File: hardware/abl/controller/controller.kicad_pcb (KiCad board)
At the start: 4 copper layers, 56.2 x 74 mm, 40 parts, among them IC2 FXL6408UMX, IC3 VEML6040A3OG, IC4 FXL6408UMX, J1 SFW20S-2STE1LF, J2 Conn_02x05_Odd_Even, J3 Conn_02x05_Odd_Even, J4 PRT-14417, J5 Conn_02x05_Odd_Even, Q2 AO3401A, Q4 AO3401A, U1 INA219AxD, U2 TXB0104RUT

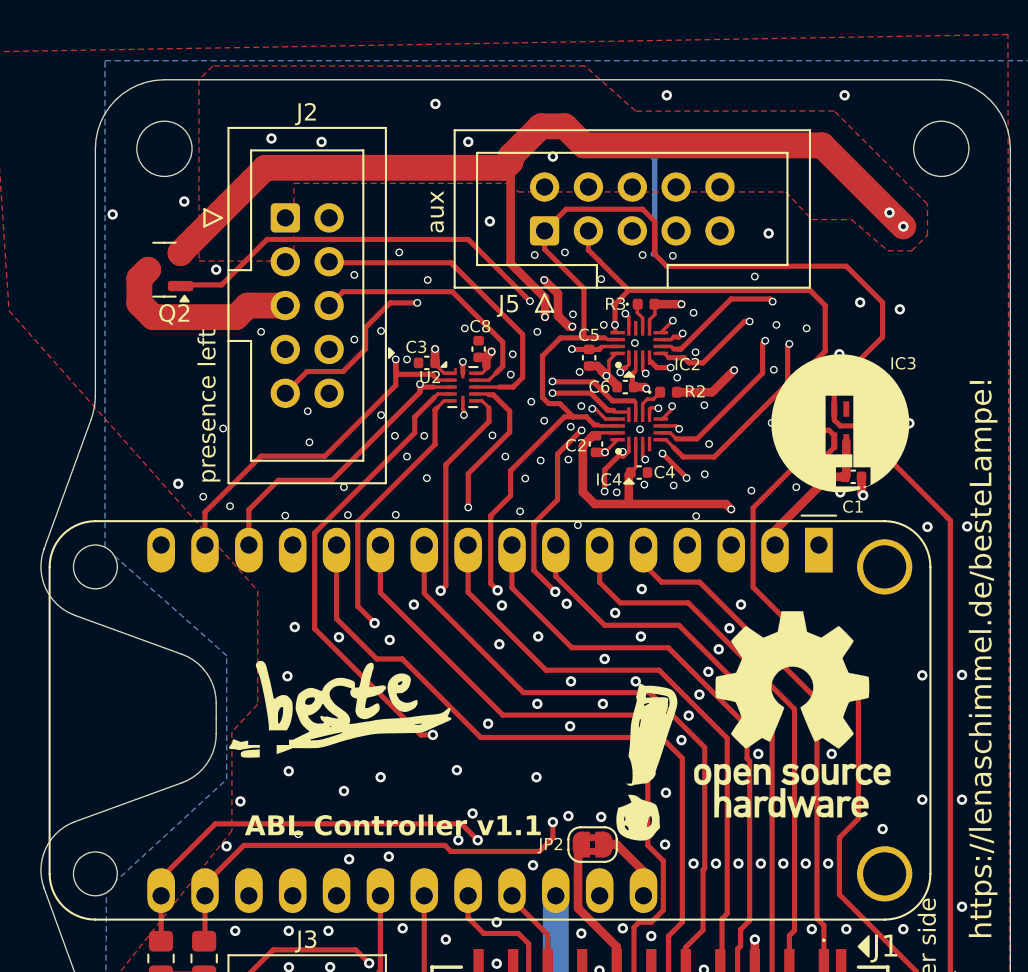
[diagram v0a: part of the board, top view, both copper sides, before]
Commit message: Exchanged GPIO Expander for one that supports 5V.
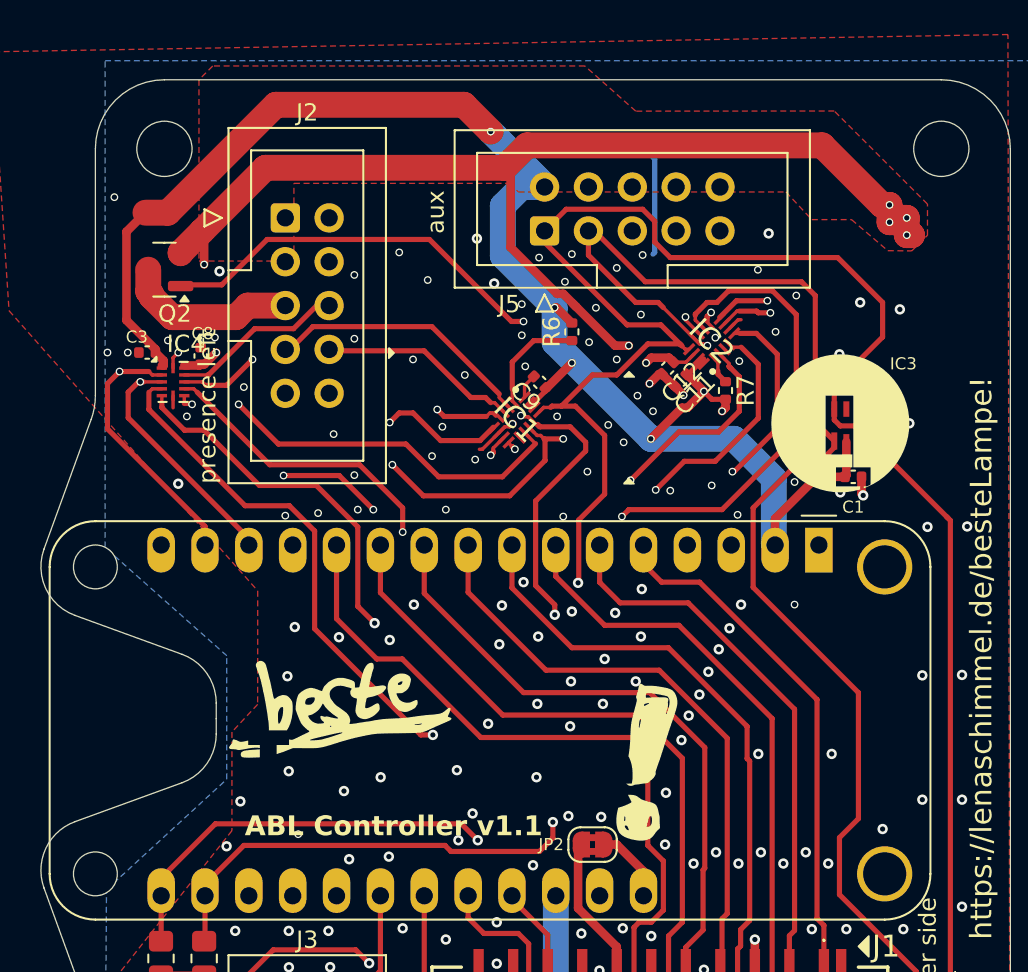
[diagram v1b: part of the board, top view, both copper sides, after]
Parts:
- removed C2, C4, C5, C6: 100nF, Capacitor_SMD:C_0402_1005Metric
- removed R2, R3: 4700R, LED_SMD:LED_0402_1005Metric
- removed REF**: OSHW-Logo_11.4x12mm_SilkScreen, Symbol:OSHW-Logo_11.4x12mm_SilkScreen
- removed U2: TXB0104RUT, Package_DFN_QFN:Texas_R-PUQFN-N12
- added C11: 100nF, Capacitor_SMD:C_0402_1005Metric, F.Cu at (96.9, 68.4)
- added C12: 100nF, Capacitor_SMD:C_0402_1005Metric, F.Cu at (96.2, 67.7)
- added C9: 100nF, Capacitor_SMD:C_0402_1005Metric, F.Cu at (88.7, 68.5)
- added IC1: TCA6408ARSVR, FXL6408UMX:QFN40P180X260X55-16N, F.Cu at (87.4, 70.7)
- added R6: 4700R, Resistor_SMD:R_0402_1005Metric, F.Cu at (90.6, 65.6)
- added R7: 4700R, Resistor_SMD:R_0402_1005Metric, F.Cu at (99.5, 69.0)
- IC2: value FXL6408UMX -> TCA6408ARSVR
- IC4: value FXL6408UMX -> TXB0104RUT; footprint FXL6408UMX:QFN40P180X260X55-16N -> Package_DFN_QFN:Texas_R-PUQFN-N12
- moved IC4 27.1 mm to (67.5, 68.5), turned to 0 degrees
- moved C3 16.2 mm to (66.0, 66.8)
- moved C8 16.1 mm to (69.1, 67.0)
- moved IC2 4.20 mm to (98.7, 66.2), turned to 135 degrees
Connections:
- IC2 pad 1: /GP_INT -> Net-(IC2-~{RESET})
- IC2 pad 10: Net-(IC2-/RST) -> /FX_5_7
- IC2 pad 11: /FX_5_1 -> /GP_INT
- IC2 pad 12: /FX_5_0 -> /SCL
- IC2 pad 13: /SCL -> /SDA
- IC2 pad 14: /SDA -> +5V
- IC2 pad 16: GND -> +3.3V
- IC2 pad 2: +5V -> /FX_5_0
- IC2 pad 3: /FX_5_7 -> /FX_5_1
- IC2 pad 4: /FX_5_6 -> /FX_5_2
- IC2 pad 5: /FX_5_5 -> /FX_5_3
- IC2 pad 6: /FX_5_4 -> GND
- IC2 pad 7: /FX_5_3 -> /FX_5_4
- IC2 pad 8: /FX_5_2 -> /FX_5_5
- IC2 pad 9: +3.3V -> /FX_5_6
- IC4 pad 1: /GP_INT -> +3.3V
- IC4 pad 10: Net-(IC4-/RST) -> /TX_L_5
- IC4 pad 11: /FX_3_1 -> +5V
- IC4 pad 12: /FX_3_0 -> /EN_UART
- IC4 pad 2: +3.3V -> /TX_L
- IC4 pad 3: /EN_UART -> /RX_L
- IC4 pad 4: /FX_3_6 -> /TX_R
- IC4 pad 5: /FX_3_5 -> /RX_R
- IC4 pad 6: /FX_3_4 -> GND
- IC4 pad 7: /FX_3_3 -> /RX_R_5
- IC4 pad 8: /FX_3_2 -> /TX_R_5
- IC4 pad 9: GND -> /RX_L_5
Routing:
- net +3.3V: track 110.2 -> 162.7 mm, vias 12 -> 11
- net /SCL: track 178.6 -> 193.9 mm, vias 5 -> 4
- net /FX_3_2: track 72.7 -> 58.1 mm
- net /FX_5_7: track 67.2 -> 81.3 mm, vias 4 -> 2
- net /FX_3_5: track 32.9 -> 19.0 mm
- net /FX_3_0: track 28.2 -> 15.5 mm, vias 1 -> 0
- net /FX_3_3: track 75.4 -> 62.9 mm
- net /RX_R_5: track 48.5 -> 57.9 mm, vias 1 -> 3
- net /FX_5_0: track 28.6 -> 38.0 mm, vias 2 -> 1
- net /FX_3_1: track 21.6 -> 12.4 mm, vias 1 -> 0
- net /EN_UART: track 18.6 -> 26.4 mm
- net GND: track 23.7 -> 31.1 mm, vias 224 -> 206
- net /GP_INT: track 31.1 -> 38.5 mm
- net Net-(IC1-~{RESET}): track 0.00 -> 6.27 mm
- net /FX_3_4: track 20.6 -> 26.2 mm
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
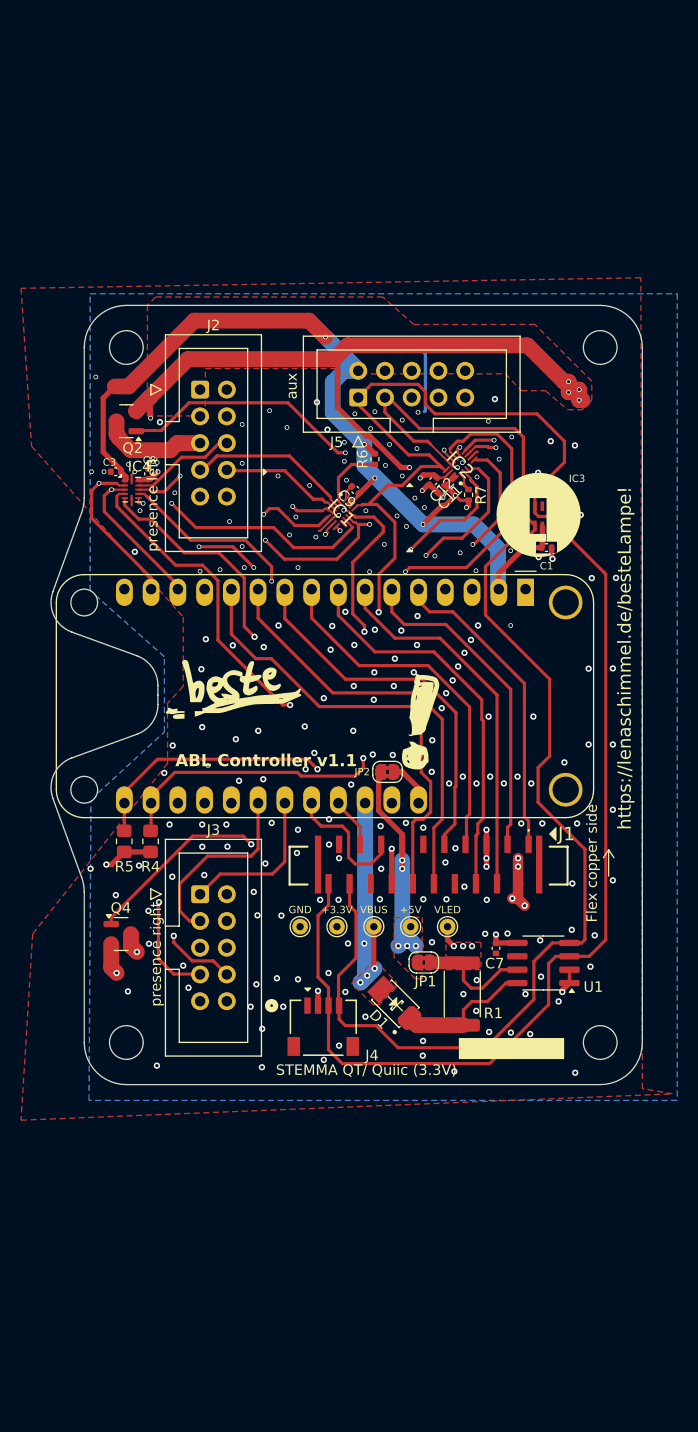
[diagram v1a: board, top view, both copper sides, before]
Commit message: Re-routed power, much cleanup.
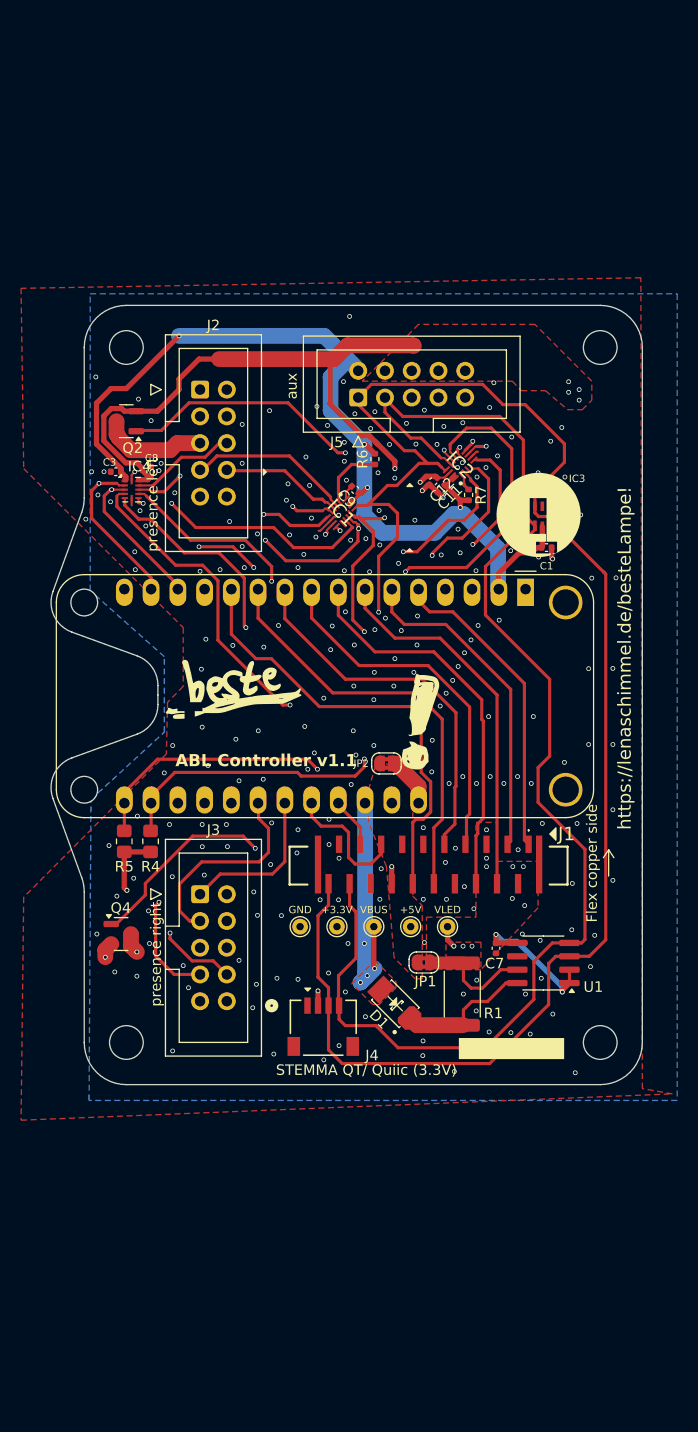
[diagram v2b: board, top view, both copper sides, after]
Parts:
- moved JP2 0.81 mm to (91.7, 94.5)
- moved C8 0.28 mm to (69.3, 66.8)
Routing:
- net GND: track 31.1 -> 9.55 mm, vias 206 -> 224
- net +5V: track 104.1 -> 113.5 mm, vias 14 -> 7
- net +4V: track 21.6 -> 12.8 mm
- net /SCL: track 193.9 -> 188.3 mm
- net +3.3V: track 162.7 -> 158.9 mm, vias 11 -> 9
- net /FX_5_5: track 10.6 -> 7.19 mm
- net /FX_5_4: track 12.8 -> 10.2 mm
- net +BATT: track 4.36 -> 6.08 mm
- net /SDA: track 201.6 -> 200.3 mm
- net /FX_3_3: track 62.9 -> 61.9 mm
- net /FX_5_7: track 81.3 -> 82.2 mm
- net /RX_R: track 55.8 -> 56.5 mm
- net /FX_5_2: track 67.7 -> 67.0 mm

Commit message: Create custom clearance rules and fix most DRC errors.
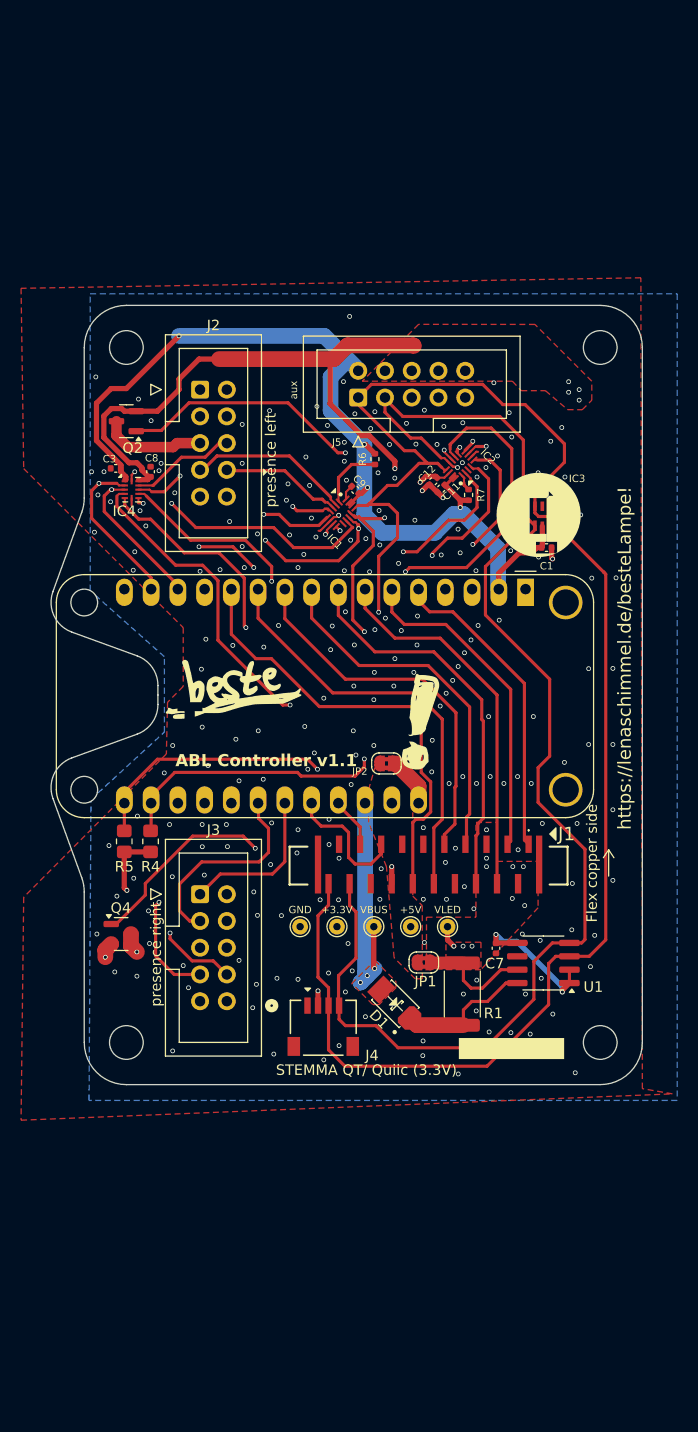
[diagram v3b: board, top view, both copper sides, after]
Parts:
- moved C3 0.32 mm to (66.0, 66.5)
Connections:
- J4 pad 5: (no net) -> GND
- J4 pad 6: (no net) -> GND

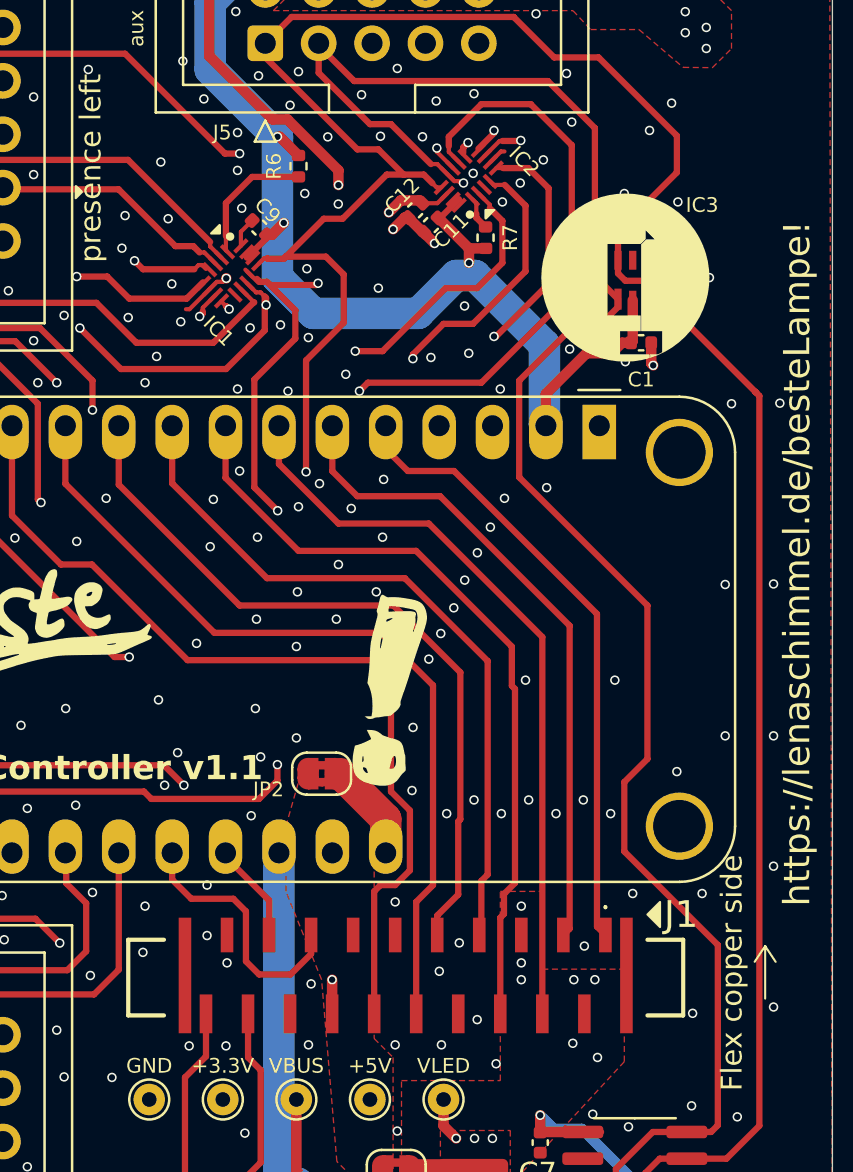
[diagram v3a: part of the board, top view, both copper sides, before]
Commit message: Fix orientation of the flex connector.
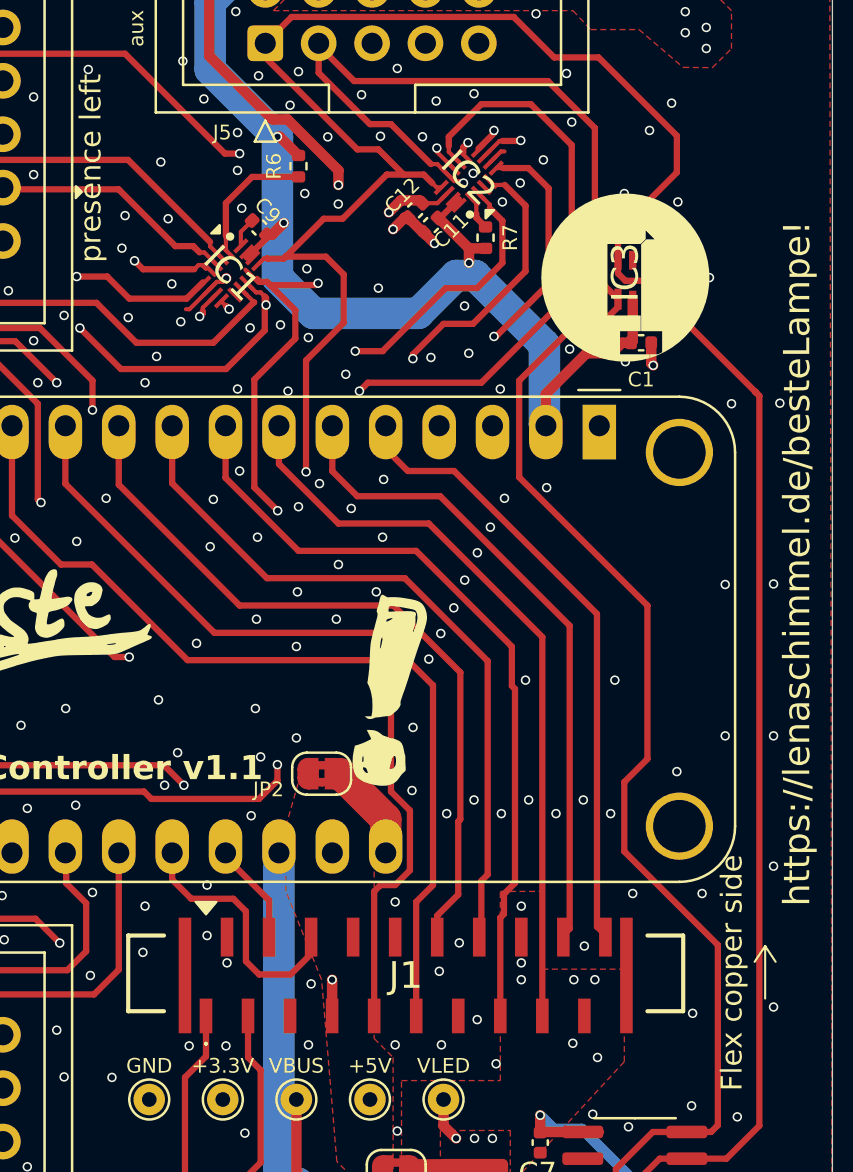
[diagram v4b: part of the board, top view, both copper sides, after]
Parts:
- J1: footprint SFW20S-2STE1LF:SFW20S2STE1LF -> Own footprints:SFW20S2STE1LF_Own
- turned J1 to 0 degrees
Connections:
- J1 pad 1: /i1 -> /SDA
- J1 pad 10: /i7 -> GND
- J1 pad 11: GND -> /i7
- J1 pad 12: /i8 -> /i6
- J1 pad 13: +5V -> GND
- J1 pad 14: +3.3V -> /i5
- J1 pad 15: /EN_LED -> /i4
- J1 pad 16: GND -> +4V
- J1 pad 17: /ALERT -> /i3
- J1 pad 18: /SCL -> /i2
- J1 pad 19: GND -> +4V
- J1 pad 2: +4V -> GND
- J1 pad 20: /SDA -> /i1
- J1 pad 3: /i2 -> /SCL
- J1 pad 4: /i3 -> /ALERT
- J1 pad 5: +4V -> GND
- J1 pad 6: /i4 -> /EN_LED
- J1 pad 7: /i5 -> +3.3V
- J1 pad 8: GND -> +5V
- J1 pad 9: /i6 -> /i8
- J4 pad 5: GND -> (no net)
- J4 pad 6: GND -> (no net)

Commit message: Several small fixes
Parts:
- moved TP1 30.8 mm to (113.8, 115.6)
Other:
- board text added: "https://beste-lampe.de"
- board text removed: "https://lenaschimmel.de/besteLampe!"
